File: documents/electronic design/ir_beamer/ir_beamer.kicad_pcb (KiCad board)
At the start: 2 copper layers, 46 parts, among them P1 Via, P10 Via, P11 Via, P12 Via, P13 Via, P14 Via, P15 Via, P16 Via, P17 Via, P2 Via, P3 Via, P4 Via, P5 Via, P6 Via, P7 Via, P8 Via, P9 Via, T1 2N7002K, T10 2N7002K, T11 2N7002K, T12 2N7002K, T2 2N7002K, T3 2N7002K, T4 2N7002K, T5 2N7002K, T6 2N7002K, T7 2N7002K, T8 2N7002K, T9 2N7002K, U1 74HC595D, U2 STM32F103HEADER, U3 74HC595D, U4 SE8R01_module

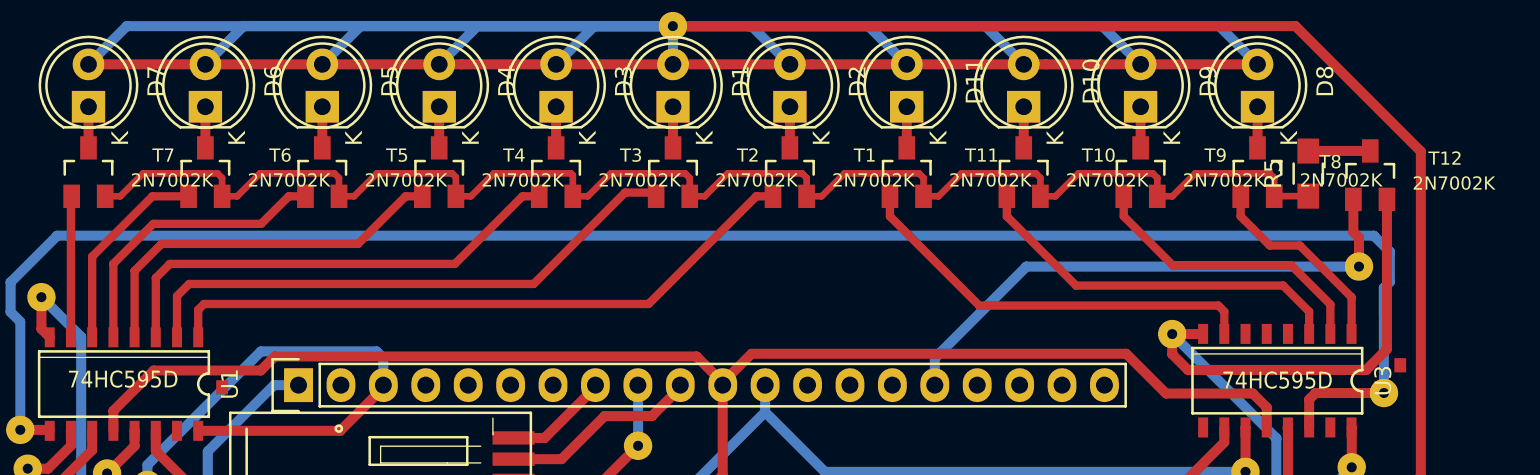
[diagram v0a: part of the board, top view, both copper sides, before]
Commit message: minor update in beamer pcb (added vias for pwm_gnd signal)
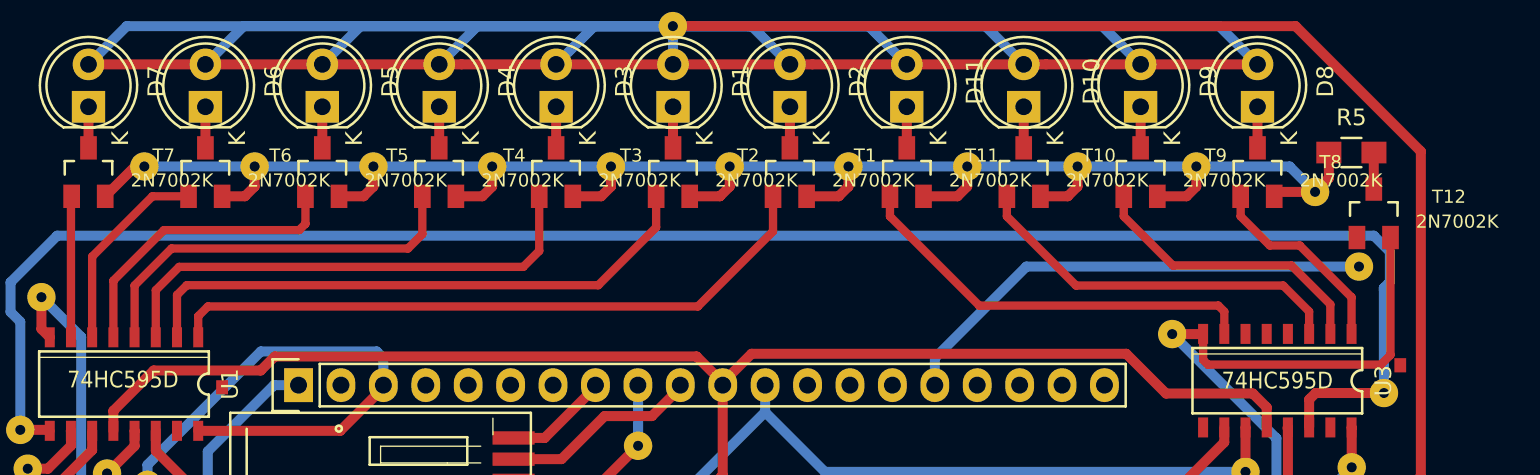
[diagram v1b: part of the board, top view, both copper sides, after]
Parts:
- added P18: Via, footprints:Via, F.Cu at (32.5, 29.5)
- added P19: Via, footprints:Via, F.Cu at (39.1, 29.5)
- added P20: Via, footprints:Via, F.Cu at (46.2, 29.5)
- added P21: Via, footprints:Via, F.Cu at (53.3, 29.5)
- added P22: Via, footprints:Via, F.Cu at (60.5, 29.5)
- added P23: Via, footprints:Via, F.Cu at (67.6, 29.5)
- added P24: Via, footprints:Via, F.Cu at (74.7, 29.5)
- added P25: Via, footprints:Via, F.Cu at (81.8, 29.5)
- added P26: Via, footprints:Via, F.Cu at (88.4, 29.5)
- added P27: Via, footprints:Via, F.Cu at (95.5, 29.5)
- added P28: Via, footprints:Via, F.Cu at (102.6, 31.0)
- moved R5 2.87 mm to (104.8, 28.6), turned to 0 degrees
- moved T12 2.29 mm to (106.1, 32.3)
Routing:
- net PWM_GND: track 90.2 -> 112.9 mm
- net IR_PWM: track 33.4 -> 29.3 mm
- net GND: track 110.2 -> 106.4 mm
- net Net-(R5-Pad2): track 3.72 -> 2.19 mm
- net IR_LED_3: track 28.5 -> 30.0 mm
- net IR_LED_2: track 33.8 -> 35.1 mm
- net IR_LED_1: track 38.9 -> 39.9 mm
- net IR_LED_4: track 23.1 -> 23.9 mm
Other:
- net class Default: clearance 0.4 -> 0.6; trace_width 0.6 -> 0.5
- rule trace_clearance: 0.4 -> 0.6

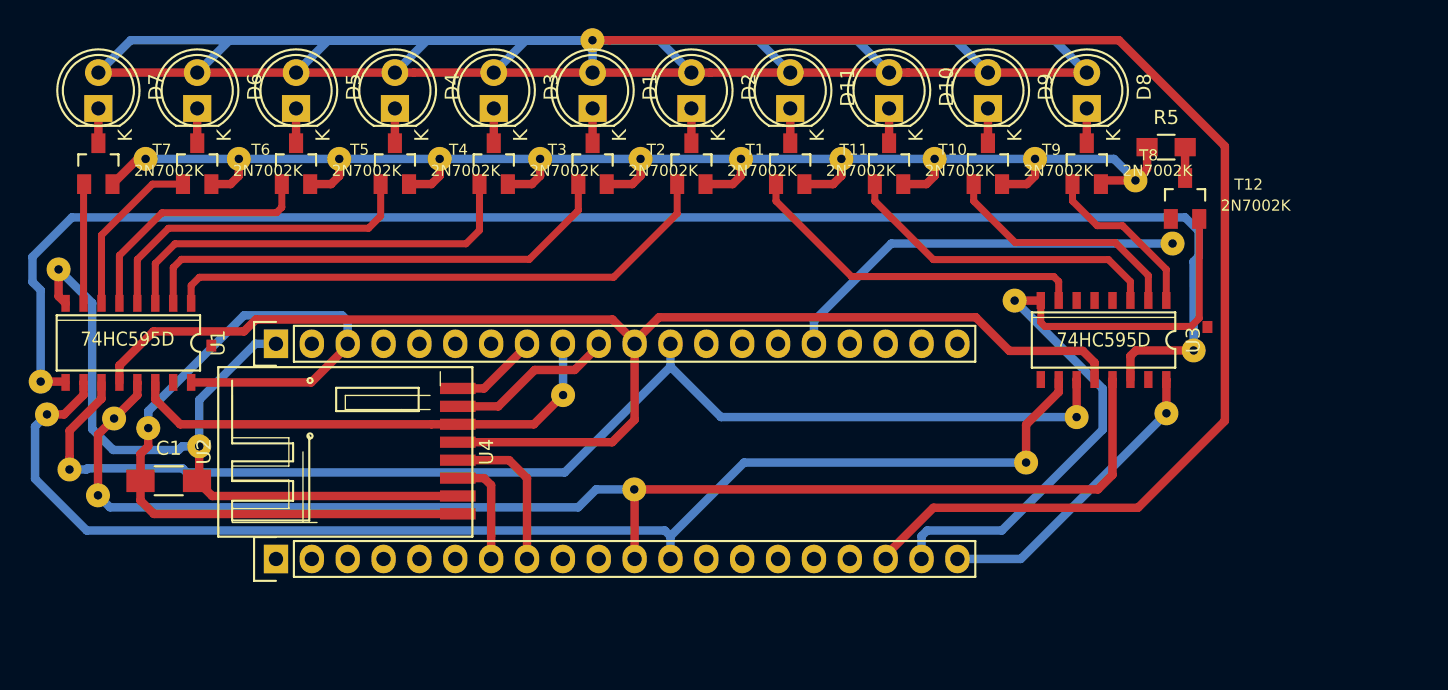
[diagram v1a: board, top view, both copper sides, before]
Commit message: remake pcb for beamer
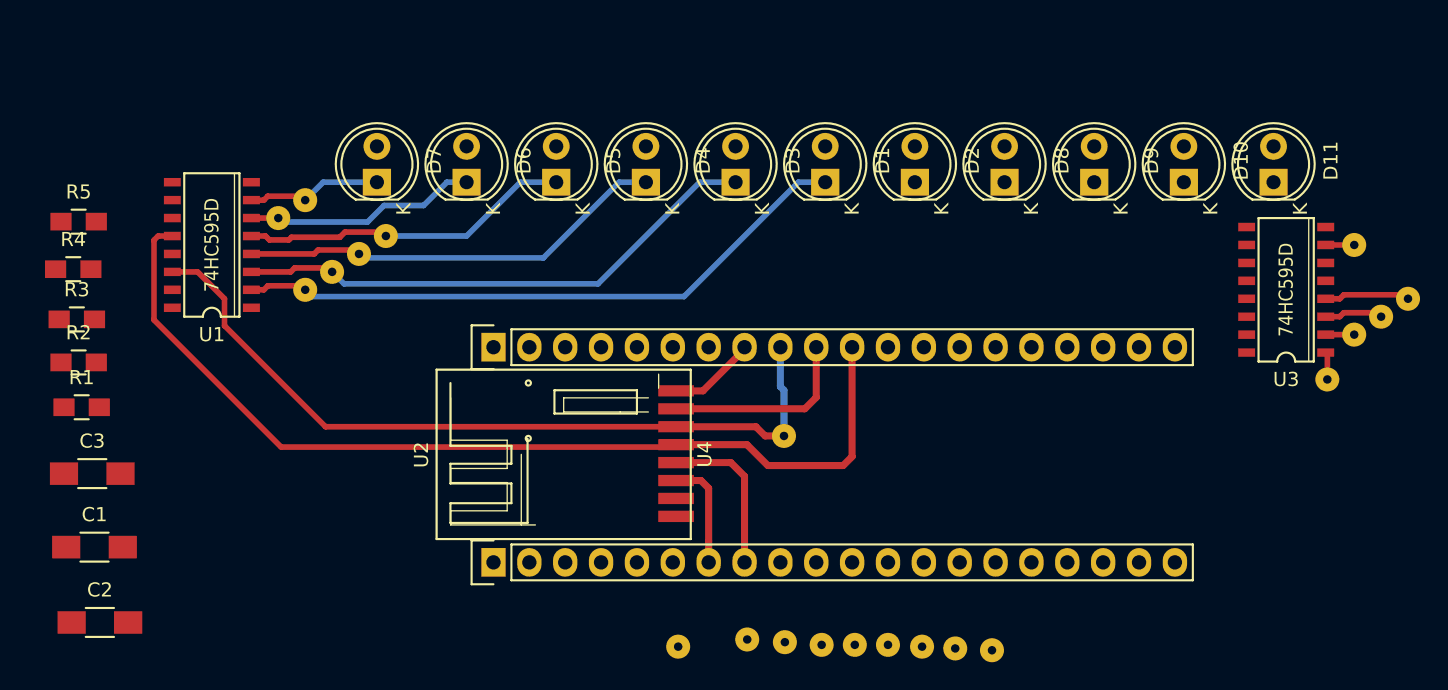
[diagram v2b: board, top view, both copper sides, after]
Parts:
- removed P22, P23, P24, P25, P26, P27, P28: Via, footprints:Via
- removed T1, T10, T11, T12, T2, T3, T4, T5, T6, T7, T8, T9: 2N7002K, footprints:SOT23
- added C2: 100uf, Capacitors_SMD:C_1206_HandSoldering, F.Cu at (29.3, 62.3)
- added C3: 100uf, Capacitors_SMD:C_1206_HandSoldering, F.Cu at (28.7, 51.8)
- added R1: 50, Capacitors_SMD:C_0805_HandSoldering, F.Cu at (28.0, 47.1)
- added R2: 10K, Capacitors_SMD:C_0805_HandSoldering, F.Cu at (27.8, 43.9)
- added R3: 10K, Capacitors_SMD:C_0805_HandSoldering, F.Cu at (27.6, 40.8)
- added R4: 10K, Capacitors_SMD:C_0805_HandSoldering, F.Cu at (27.4, 37.3)
- R5: value 100 -> 10K; footprint Resistors_SMD:R_0805_HandSoldering -> Capacitors_SMD:C_0805_HandSoldering
- moved P18 86.5 mm to (118.1, 41.9)
- moved P19 81.7 mm to (120.0, 40.6)
- moved P4 80.0 mm to (116.2, 45.1)
- moved R5 77.2 mm to (27.8, 33.9)
- moved P20 76.3 mm to (121.9, 39.4)
- moved P10 68.9 mm to (89.9, 64.1)
- moved P21 65.1 mm to (118.1, 35.6)
- moved P8 62.8 mm to (85.1, 63.9)
- moved P16 50.7 mm to (43.8, 32.4)
- moved P5 50.1 mm to (80.4, 63.9)
- moved P2 49.5 mm to (75.1, 63.5)
- moved P13 48.1 mm to (49.5, 34.9)
- moved P17 43.4 mm to (70.2, 64.0)
- moved P3 39.4 mm to (77.8, 63.7)
- moved D11 34.6 mm to (112.4, 31.1)
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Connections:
- D1 pad 1: Net-(D1-Pad1) -> IR_LED_2
- D1 pad 2: +5V -> IR_VCC
- D10 pad 1: Net-(D10-Pad1) -> IR_LED_10
- D10 pad 2: +5V -> IR_VCC
- D11 pad 1: Net-(D11-Pad1) -> IR_LED_DATA
- D11 pad 2: +5V -> IR_VCC
- D2 pad 1: Net-(D2-Pad1) -> IR_LED_1
- D2 pad 2: +5V -> IR_VCC
- D3 pad 1: Net-(D3-Pad1) -> IR_LED_3
- D3 pad 2: +5V -> IR_VCC
- D4 pad 1: Net-(D4-Pad1) -> IR_LED_4
- D4 pad 2: +5V -> IR_VCC
- D5 pad 1: Net-(D5-Pad1) -> IR_LED_5
- D5 pad 2: +5V -> IR_VCC
- D6 pad 1: Net-(D6-Pad1) -> IR_LED_6
- D6 pad 2: +5V -> IR_VCC
- D7 pad 1: Net-(D7-Pad1) -> IR_LED_7
- D7 pad 2: +5V -> IR_VCC
- D8 pad 1: Net-(D8-Pad1) -> IR_LED_8
- D8 pad 2: +5V -> IR_VCC
- D9 pad 1: Net-(D9-Pad1) -> IR_LED_9
- D9 pad 2: +5V -> IR_VCC
- P11 pad 1: MR_NOT -> IR_LED_3
- P12 pad 1: OE_NOT -> IR_LED_4
- P13 pad 1: MR_NOT -> IR_LED_5
- P15 pad 1: OE_NOT -> IR_LED_6
- P16 pad 1: GND -> IR_LED_7
- P18 pad 1: PWM_GND -> IR_LED_8
- P19 pad 1: PWM_GND -> IR_LED_9
- P20 pad 1: PWM_GND -> IR_LED_10
- P21 pad 1: PWM_GND -> IR_LED_DATA
- P4 pad 1: GND -> IR_LED_1
- P6 pad 1: OE_NOT -> IR_LED_2
- R5 pad 1: PWM_GND -> +3V3
- R5 pad 2: Net-(R5-Pad2) -> IR_PWM
- U1 pad 1: IR_LED_1 -> (no net)
- U1 pad 10: MR_NOT -> Net-(R2-Pad2)
- U1 pad 13: OE_NOT -> IR_PWM
- U2 pad 11: OE_NOT -> (no net)
- U2 pad 12: MR_NOT -> (no net)
- U3 pad 1: IR_LED_8 -> IR_LED_1
- U3 pad 10: MR_NOT -> Net-(R3-Pad2)
- U3 pad 13: OE_NOT -> IR_PWM
- U3 pad 2: IR_LED_9 -> IR_LED_8
- U3 pad 3: IR_LED_10 -> IR_LED_9
- U3 pad 4: (no net) -> IR_LED_10
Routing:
- net +5V: track 382.9 -> 0.00 mm
- net PWM_GND: track 112.9 -> 0.00 mm
- net Cascade: track 109.9 -> 0.00 mm
- net GND: track 106.4 -> 0.00 mm
- net OE_NOT: track 94.2 -> 0.00 mm
- net MR_NOT: track 91.6 -> 0.00 mm
- net Latch: track 87.9 -> 0.00 mm
- net +3V3: track 82.1 -> 0.00 mm
- net IR_LED_1: track 39.9 -> 1.95 mm
- net IR_PWM: track 29.3 -> 0.00 mm
- net SPI_SCK: track 94.2 -> 68.9 mm
- net IR_LED_DATA: track 24.9 -> 2.66 mm
- net SPI_MOSI: track 35.3 -> 55.6 mm
- net IR_LED_10: track 23.0 -> 6.06 mm
- net IR_LED_9: track 17.5 -> 4.16 mm
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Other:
- net class Default: clearance 0.6 -> 0.5; trace_width 0.5 -> 0.4
- rule trace_clearance: 0.6 -> 0.5
- board text removed: "."

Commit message: update pcb for beamer
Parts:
- removed P1, P10, P11, P12, P13, P14, P15, P16, P17, P18, P19, P2, P20, P21, P3, P4, P5, P6, P7, P8, P9: Via, footprints:Via
- moved R1 70.1 mm to (97.2, 58.4), turned to 270 degrees
- moved R5 70.0 mm to (97.0, 44.6), turned to 180 degrees
- moved R3 60.4 mm to (87.9, 36.6), turned to 270 degrees
- moved C1 59.2 mm to (84.7, 37.3), turned to 90 degrees
- moved R4 42.1 mm to (69.3, 41.2), turned to 270 degrees
- moved R2 30.0 mm to (57.7, 43.2)
- moved C3 27.8 mm to (52.9, 38.1), turned to 90 degrees
- moved U1 25.8 mm to (62.9, 38.2), turned to 180 degrees
- moved D11 25.4 mm to (87.0, 31.1)
- moved D2 25.4 mm to (112.4, 31.1)
- moved U3 18.9 mm to (94.4, 38.2), turned to 180 degrees
- moved C2 18.3 mm to (47.0, 57.8), turned to 90 degrees
- moved D10 12.7 mm to (93.3, 31.1)
- moved D8 12.7 mm to (106.0, 31.1)
- moved U4 5.59 mm to (68.0, 61.0)
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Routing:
- net IR_VCC: track 0.00 -> 205.5 mm, vias 0 -> 2
- net +3V3: track 0.00 -> 177.2 mm, vias 0 -> 10
- net GND: track 0.00 -> 141.9 mm, vias 0 -> 4
- net Cascade: track 0.00 -> 44.2 mm, vias 0 -> 2
- net IR_PWM: track 0.00 -> 41.9 mm, vias 0 -> 2
- net Latch: track 0.00 -> 41.5 mm, vias 0 -> 4
- net IR_LED_2: track 44.4 -> 16.7 mm
- net IR_LED_3: track 37.9 -> 11.9 mm
- net SPI_MOSI: track 55.6 -> 30.4 mm, vias 0 -> 2
- net IR_LED_4: track 30.5 -> 7.03 mm
- net IR_LED_5: track 23.6 -> 4.58 mm
- net IR_LED_1: track 1.95 -> 15.6 mm
- net IR_LED_8: track 2.02 -> 10.9 mm
- net IR_LED_6: track 16.5 -> 9.16 mm
- net Net-(R3-Pad2): track 0.00 -> 6.03 mm
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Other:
- net class Default: clearance 0.5 -> 0.4; trace_width 0.4 -> 0.5; via_dia 0.6 -> 0.9
- rule trace_clearance: 0.5 -> 0.4

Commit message: fix beamer pcb
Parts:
- R1: value 50 -> 22
- moved R1 4.25 mm to (96.8, 54.1)
- moved D1 2.54 mm to (80.6, 28.6), turned to 270 degrees
- moved D10 2.54 mm to (93.3, 28.6), turned to 270 degrees
- moved D11 2.54 mm to (87.0, 28.6), turned to 270 degrees
- moved D2 2.54 mm to (112.4, 28.6), turned to 270 degrees
- moved D3 2.54 mm to (74.3, 28.6), turned to 270 degrees
- moved D4 2.54 mm to (67.9, 28.6), turned to 270 degrees
- moved D5 2.54 mm to (61.6, 28.6), turned to 270 degrees
- moved D6 2.54 mm to (55.2, 28.6), turned to 270 degrees
- moved D7 2.54 mm to (48.9, 28.6), turned to 270 degrees
- moved D8 2.54 mm to (106.0, 28.6), turned to 270 degrees
- moved D9 2.54 mm to (99.7, 28.6), turned to 270 degrees
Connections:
- D1 pad 1: IR_LED_2 -> IR_GND
- D1 pad 2: IR_VCC -> IR_LED_2
- D10 pad 1: IR_LED_10 -> IR_GND
- D10 pad 2: IR_VCC -> IR_LED_10
- D11 pad 1: IR_LED_DATA -> IR_GND
- D11 pad 2: IR_VCC -> IR_LED_DATA
- D2 pad 1: IR_LED_1 -> IR_GND
- D2 pad 2: IR_VCC -> IR_LED_1
- D3 pad 1: IR_LED_3 -> IR_GND
- D3 pad 2: IR_VCC -> IR_LED_3
- D4 pad 1: IR_LED_4 -> IR_GND
- D4 pad 2: IR_VCC -> IR_LED_4
- D5 pad 1: IR_LED_5 -> IR_GND
- D5 pad 2: IR_VCC -> IR_LED_5
- D6 pad 1: IR_LED_6 -> IR_GND
- D6 pad 2: IR_VCC -> IR_LED_6
- D7 pad 1: IR_LED_7 -> IR_GND
- D7 pad 2: IR_VCC -> IR_LED_7
- D8 pad 1: IR_LED_8 -> IR_GND
- D8 pad 2: IR_VCC -> IR_LED_8
- D9 pad 1: IR_LED_9 -> IR_GND
- D9 pad 2: IR_VCC -> IR_LED_9
- R1 pad 1: IR_VCC -> IR_GND
- R1 pad 2: +5V -> GND
- U2 pad 18: +5V -> (no net)
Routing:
- net IR_VCC: track 205.5 -> 0.00 mm, vias 2 -> 0
- net IR_GND: track 0.00 -> 202.8 mm, vias 0 -> 2
- net GND: track 141.9 -> 150.6 mm
- net +5V: track 3.10 -> 0.00 mm
- net IR_LED_DATA: track 6.93 -> 7.81 mm
- net IR_LED_9: track 6.66 -> 5.91 mm
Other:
- net class Default: via_dia 0.9 -> 1.2

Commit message: fix beamer pcb
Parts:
- moved R1 22.9 mm to (111.2, 36.3), turned to 180 degrees
- moved R5 4.86 mm to (101.2, 42.3), turned to 270 degrees
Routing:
- net IR_GND: track 202.8 -> 74.7 mm, vias 2 -> 0
- net +3V3: track 177.2 -> 151.1 mm, vias 10 -> 6
- net GND: track 150.6 -> 140.2 mm, vias 4 -> 2
- net Cascade: track 44.2 -> 51.4 mm
- net IR_PWM: track 42.3 -> 47.1 mm, vias 2 -> 0
- net SPI_MOSI: track 30.4 -> 32.2 mm, vias 2 -> 4
- net Latch: track 41.5 -> 42.1 mm, vias 4 -> 3
- net SPI_SCK: track 63.1 -> 62.9 mm, vias 5 -> 2

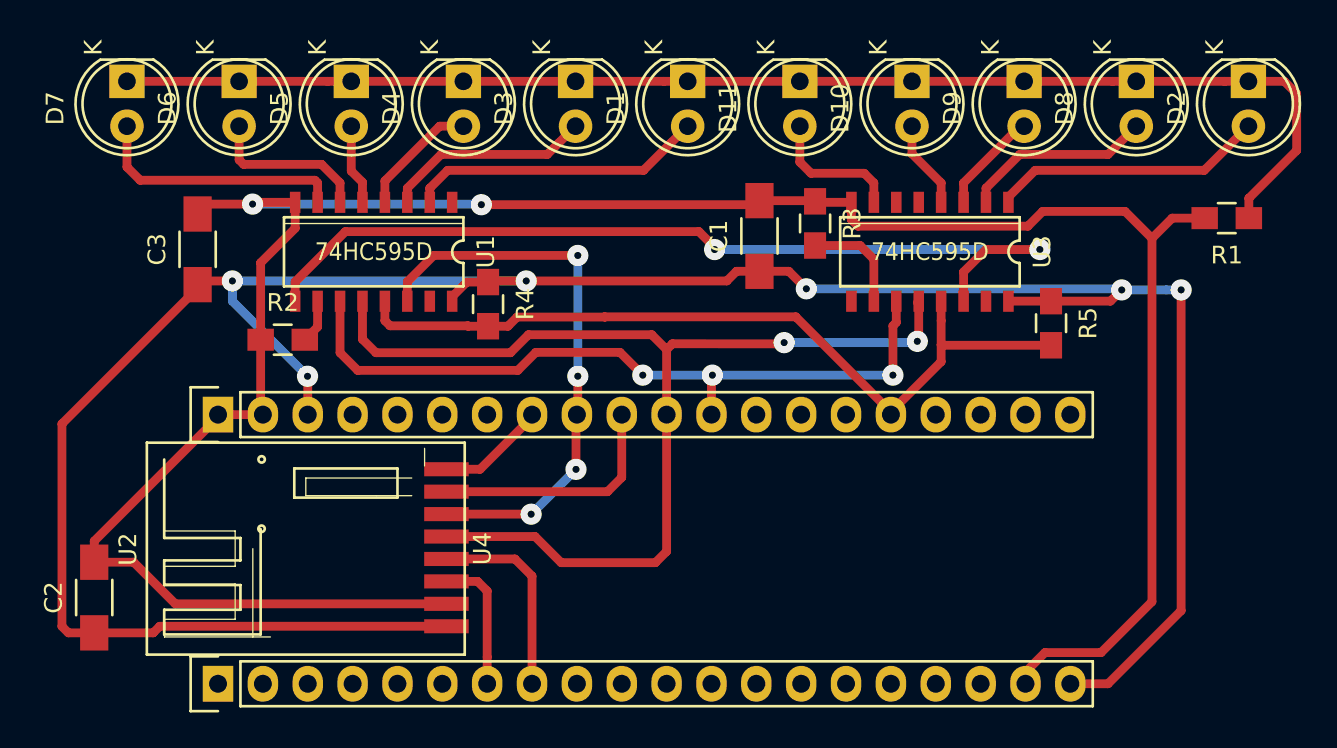
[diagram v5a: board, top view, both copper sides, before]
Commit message: increase thicknesse of routes and vias in beamer pcb
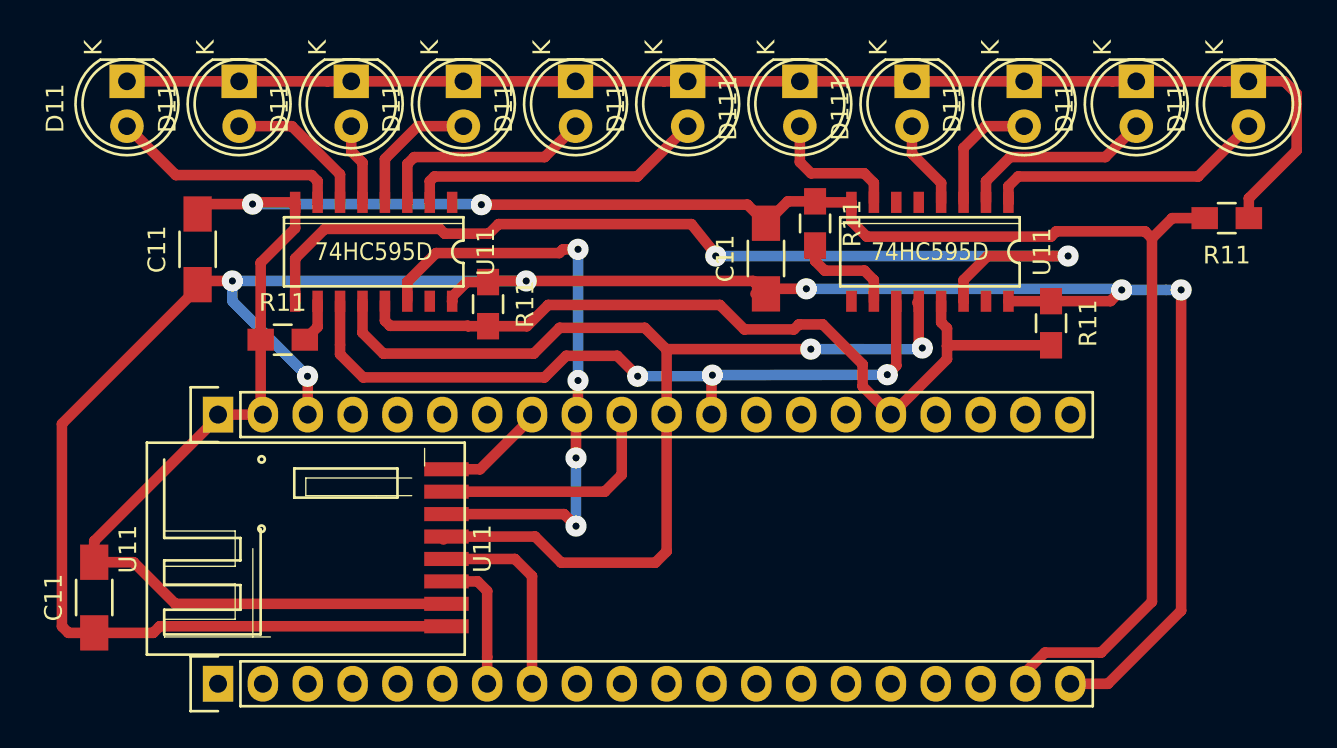
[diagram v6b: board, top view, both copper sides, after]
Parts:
- moved C11 1.33 mm to (85.1, 38.6)
- renumbered C1 to C11, C2 to C11, C3 to C11, D1 to D11, D2 to D11, D3 to D11, D4 to D11, D5 to D11, D6 to D11, D7 to D11, D8 to D11, D9 to D11, D10 to D111, D11 to D111, R2 to R11, R3 to R11, R4 to R11, R5 to R11, R1 to R11, U3 to U11, U2 to U11, U1 to U11, U4 to U11
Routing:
- net Cascade: track 51.4 -> 55.8 mm
- net SPI_MOSI: track 32.2 -> 35.1 mm
- net IR_PWM: track 47.1 -> 48.7 mm
- net IR_LED_9: track 5.91 -> 7.29 mm
- net IR_LED_7: track 14.6 -> 13.3 mm
- net SPI_SCK: track 62.9 -> 63.9 mm
- net IR_LED_6: track 9.26 -> 8.43 mm
- net GND: track 140.2 -> 141.1 mm
- net IR_LED_3: track 11.8 -> 12.6 mm
- net IR_LED_4: track 6.94 -> 7.67 mm
- net IR_LED_1: track 15.6 -> 16.2 mm
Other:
- net class Default: trace_width 0.5 -> 0.6
- net class IR_GND added: clearance 0.6, trace_width 0.8, via_dia 1.2, via_drill 0.4
